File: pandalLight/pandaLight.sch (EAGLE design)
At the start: 113 parts, among them J1 PJ-037A, U13 TPD12S016PWR, U15 PMOD-2X6, U16 PMOD-2X6, U17 PLR135-T10, U18 PLT133-T10W, U20 TP10SQ, U21 TP10SQ, U22 PAN1322, U23 6SLX9TQG144, U4 FT2232HL, U5 93LC46BT-I/OT, U6 51, U7 51, U8 TPD12S016PWR, X1 USBUB-S, X2 HDMI_RECEPTICAL_A, X4 HDMI_RECEPTICAL_A, Y1 403, Y2 20Mhz

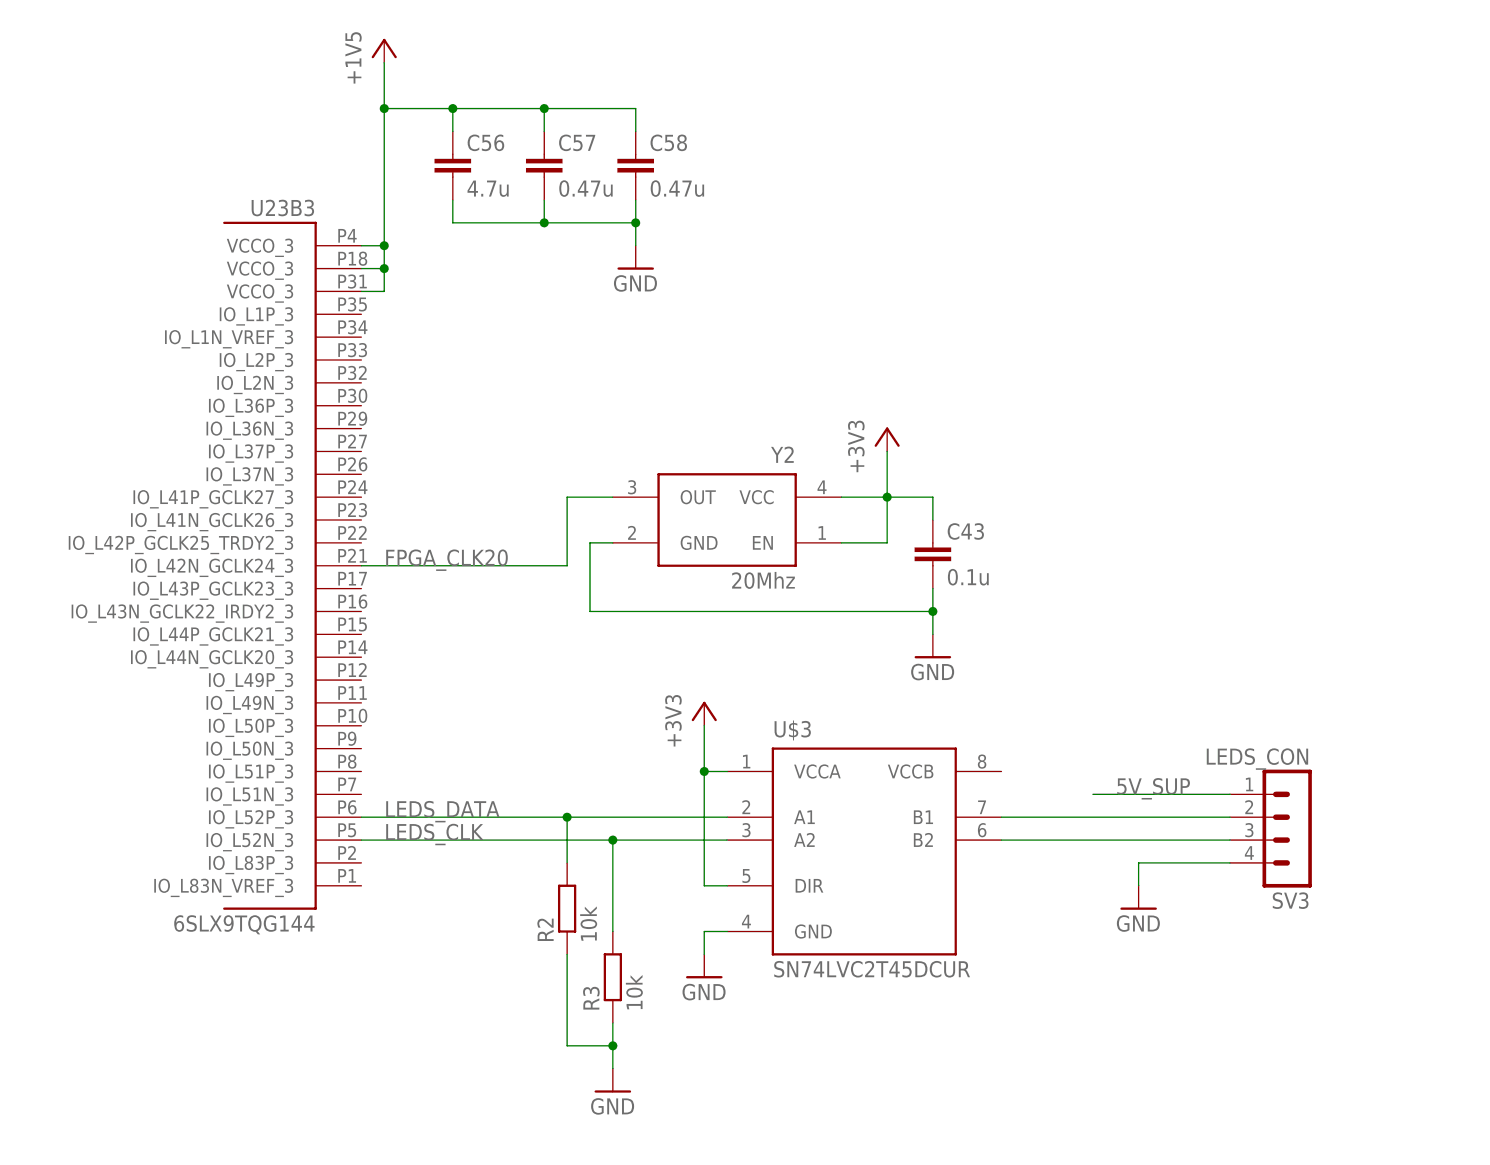
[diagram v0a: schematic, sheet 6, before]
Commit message: Added second LED strip connector; Switched to 4-Bit level shifter
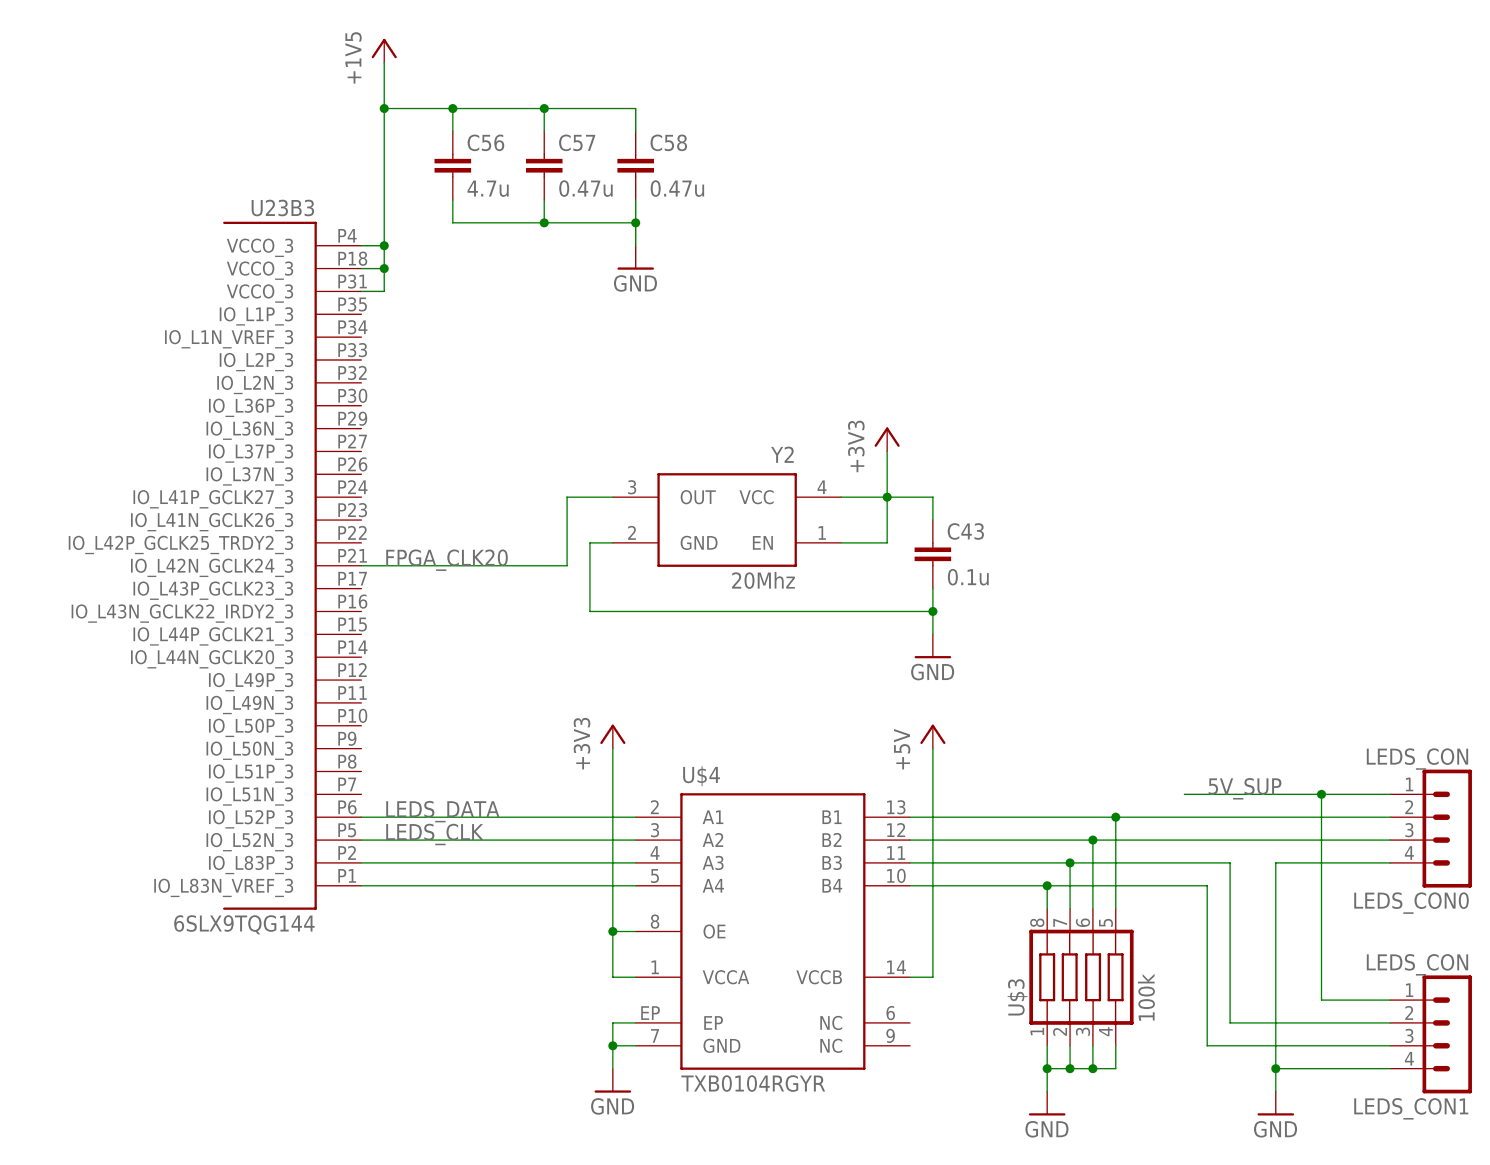
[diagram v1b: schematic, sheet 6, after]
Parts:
- removed R2, R3: 10k, pandaLight:RESISTOR0402
- removed SV3: LEDS_CON, pandaLight:MA04-1
- added LEDS_CON0, LEDS_CON1: LEDS_CON, pandaLight:MA04-1
- added U$4: TXB0104RGYR, pandaLight:TXB0104RGYR
- U$3: value SN74LVC2T45DCUR -> 100k; device pandaLight:SN74LVC2T45DCUR -> pandaLight:741C083
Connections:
- removed net N$2: SV3.2, U$3.B1
- new net N$16: U$4.A3, U23B3.IO_L83P_3
- new net N$17: U$4.A4, U23B3.IO_L83N_VREF_3
- new net N$18: LEDS_CON0.2, U$3.5, U$4.B1
- new net N$21: LEDS_CON1.2, U$3.7, U$4.B3
- new net N$22: LEDS_CON1.3, U$3.8, U$4.B4
- net +3V3: now also U$4.OE, U$4.VCCA, U6.5, U6.6, U6.7, U6.8, U7.5, U7.6, U7.7, U7.8; no longer U$3.DIR, U$3.VCCA, U6.13, U6.15, U6.16, U6.C3, U7.13, U7.15, U7.16, U7.C3
- net +5V: now also U$4.VCCB
- net 5V_SUP: now also LEDS_CON0.1, LEDS_CON1.1; no longer SV3.1
- net GND: now also LEDS_CON0.4, LEDS_CON1.4, U$3.1, U$3.2, U$3.3, U$3.4, U$4.EP, U$4.GND; no longer R2.1, R3.1, SV3.4, U$3.GND
- net LEDS_CLK: now also U$4.A2; no longer R3.2, U$3.A2
- net LEDS_DATA: now also U$4.A1; no longer R2.2, U$3.A1
- net N$3: now also LEDS_CON0.3, U$3.6, U$4.B2; no longer SV3.3, U$3.B2

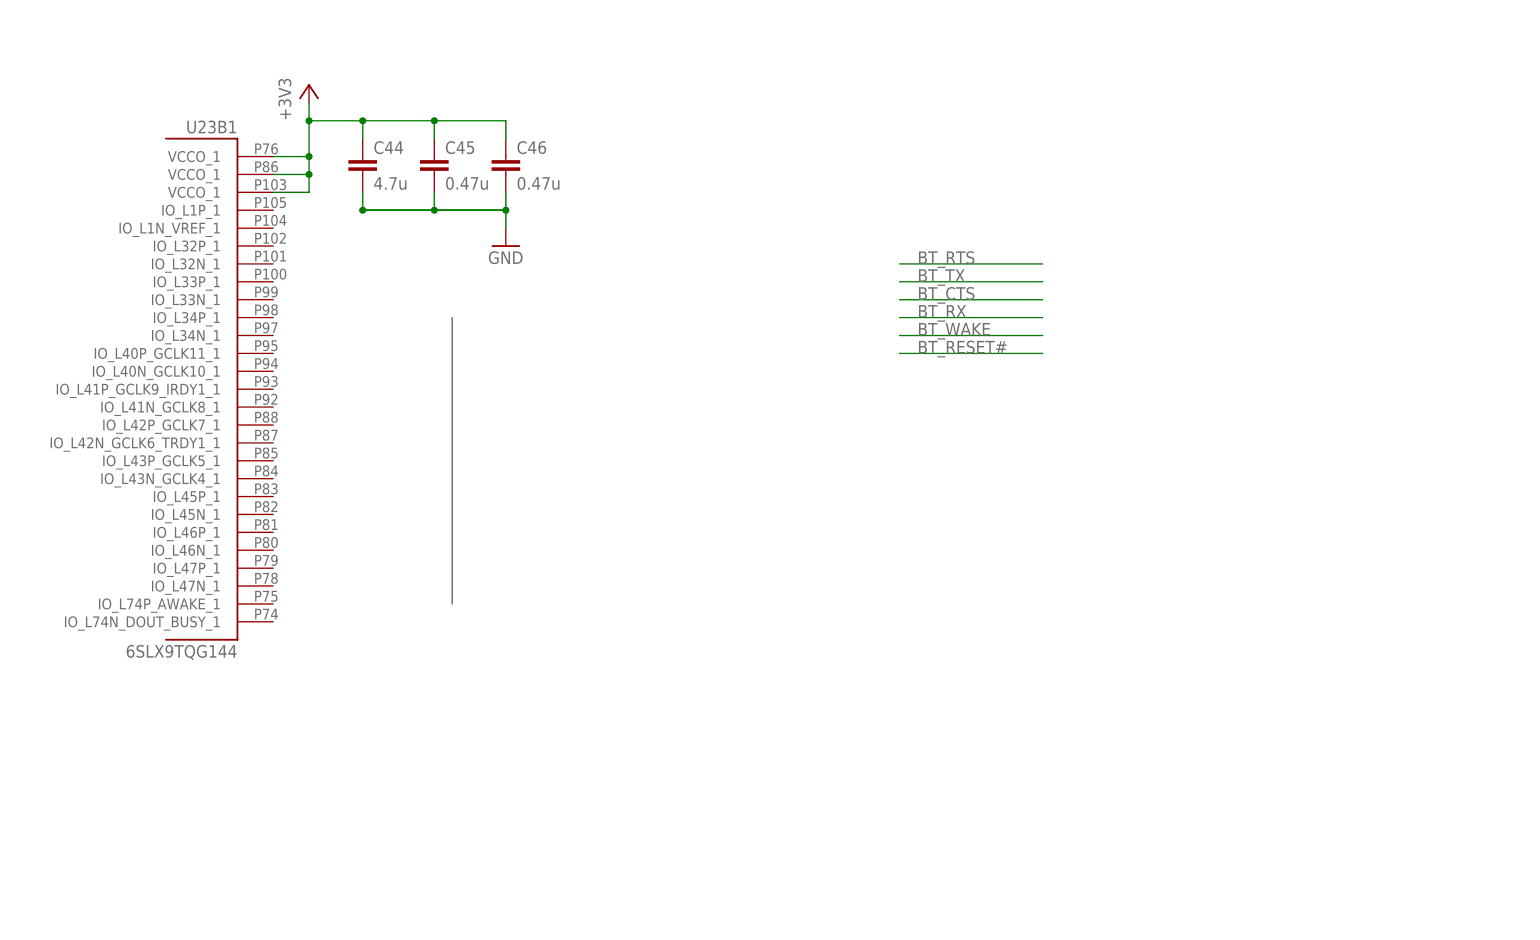
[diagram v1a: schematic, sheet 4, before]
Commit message: Routed USB to FPGA signals
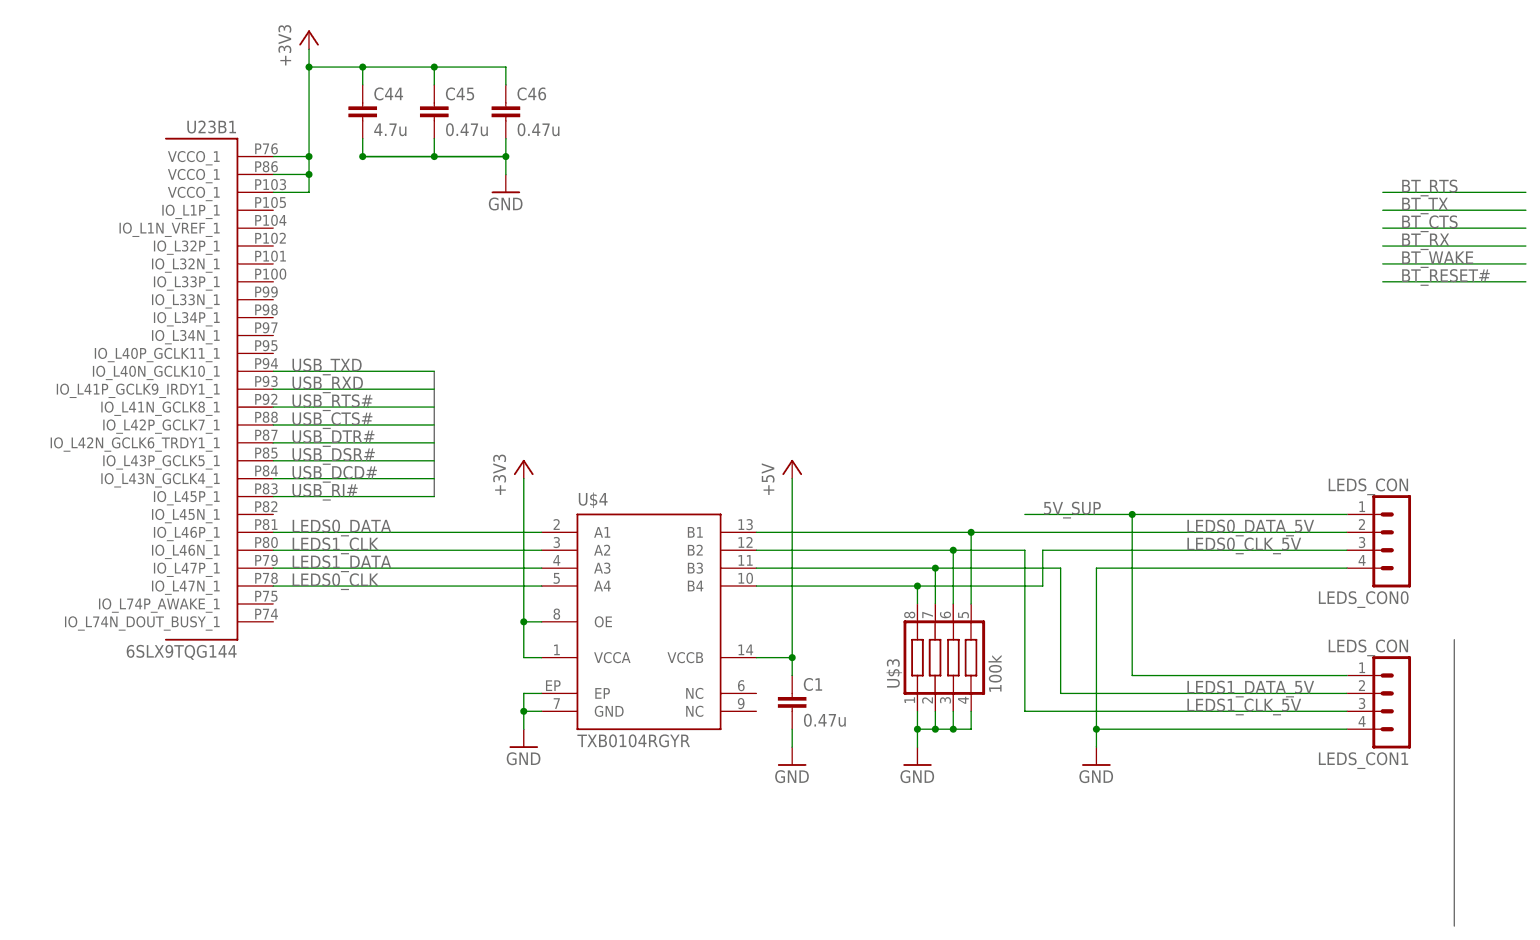
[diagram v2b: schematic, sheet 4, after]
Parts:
- added C1: 0.47u, pandaLight:CAPACITOR0402
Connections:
- net N$18 renamed LEDS0_DATA_5V
- net N$21 renamed LEDS1_DATA_5V
- removed net LEDS_CLK: U$4.A2, U23B3.IO_L52N_3
- removed net LEDS_DATA: U$4.A1, U23B3.IO_L52P_3
- removed net N$16: U$4.A3, U23B3.IO_L83P_3
- removed net N$17: U$4.A4, U23B3.IO_L83N_VREF_3
- removed net N$22: LEDS_CON1.3, U$3.8, U$4.B4
- removed net N$3: LEDS_CON0.3, U$3.6, U$4.B2
- new net LEDS0_CLK: U$4.A4, U23B1.IO_L47N_1
- new net LEDS0_CLK_5V: LEDS_CON0.3, U$3.8, U$4.B4
- new net LEDS0_DATA: U$4.A1, U23B1.IO_L46P_1
- new net LEDS1_CLK: U$4.A2, U23B1.IO_L46N_1
- new net LEDS1_CLK_5V: LEDS_CON1.3, U$3.6, U$4.B2
- new net LEDS1_DATA: U$4.A3, U23B1.IO_L47P_1
- net +5V: now also C1.1
- net GND: now also C1.2
- net USB_CTS#: now also U23B1.IO_L42P_GCLK7_1; no longer U23B0.IO_L66N_SCP0_0
- net USB_DCD#: now also U23B1.IO_L43N_GCLK4_1; no longer U23B0.IO_L63N_SCP6_0
- net USB_DSR#: now also U23B1.IO_L43P_GCLK5_1; no longer U23B0.IO_L64P_SCP5_0
- net USB_DTR#: now also U23B1.IO_L42N_GCLK6_TRDY1_1; no longer U23B0.IO_L64N_SCP4_0
- net USB_RI#: now also U23B1.IO_L45P_1; no longer U23B0.IO_L63P_SCP7_0
- net USB_RTS#: now also U23B1.IO_L41N_GCLK8_1; no longer U23B0.IO_L66P_SCP1_0
- net USB_RXD: now also U23B1.IO_L41P_GCLK9_IRDY1_1; no longer U23B0.IO_L65N_SCP2_0
- net USB_TXD: now also U23B1.IO_L40N_GCLK10_1; no longer U23B0.IO_L65P_SCP3_0
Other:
- moved on the sheet: C44, C45, C46
